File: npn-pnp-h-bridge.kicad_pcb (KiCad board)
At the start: 2 copper layers, 45 x 19 mm, 35 parts, among them J1 S4B-PH-K-S_LF__SN_, J2 S2B-PH-K-S_LF__SN_, Q1 MMDT3904, Q2 MMDT3904

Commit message: Add 1.0 revision number, use current screenshots, add exported case
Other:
- board text added: "${COMMENT1}"
- board text added: "H-Bridge for Fairylights ${REVISION}"
- board text removed: "H-Bridge for Fairylights"
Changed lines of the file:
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@@
 	)
 	(paper "A4")
+	(title_block
+		(rev "1.0")
+		(comment 1 "https://github.com/lk-ek/npn-pnp-h-bridge/")
+	)
 	(layers
 		(0 "F.Cu" signal)
@@
 		)
 	)
-	(gr_text "H-Bridge for Fairylights"
-		(at 110.83841 67.360437 0)
+	(gr_text "${COMMENT1}"
+		(at 110.2 51.2 0)
 		(layer "B.SilkS" knockout)
 		(effects
 			(font
-				(size 1 1)
+				(size 0.8 0.8)
+				(thickness 0.1)
+			)
+			(justify bottom mirror)
+		)
+	)
+	(gr_text "H-Bridge for Fairylights ${REVISION}"
+		(at 110.83841 67.6 0)
+		(layer "B.SilkS" knockout)
+		(effects
+			(font
+				(size 0.8 0.8)
 				(thickness 0.1)
 			)

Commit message: update pcb with new values
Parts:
- R11, R12: value 680 -> 2.2k
- R13, R14: value 100 -> 180

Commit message: first 4-layer try
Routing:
- net GND: track 6.69 -> 13.1 mm, vias 26 -> 10
- net /O2: track 4.20 -> 0.00 mm, vias 1 -> 0
- added copper zone on F.Cu, net /O1
- added copper zone on F.Cu, net /O2
- added copper zone on In1.Cu, net GND
- added copper zone on In2.Cu, net GND
- removed copper zone on F.Cu, net GND
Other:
- copper layers 2 -> 4

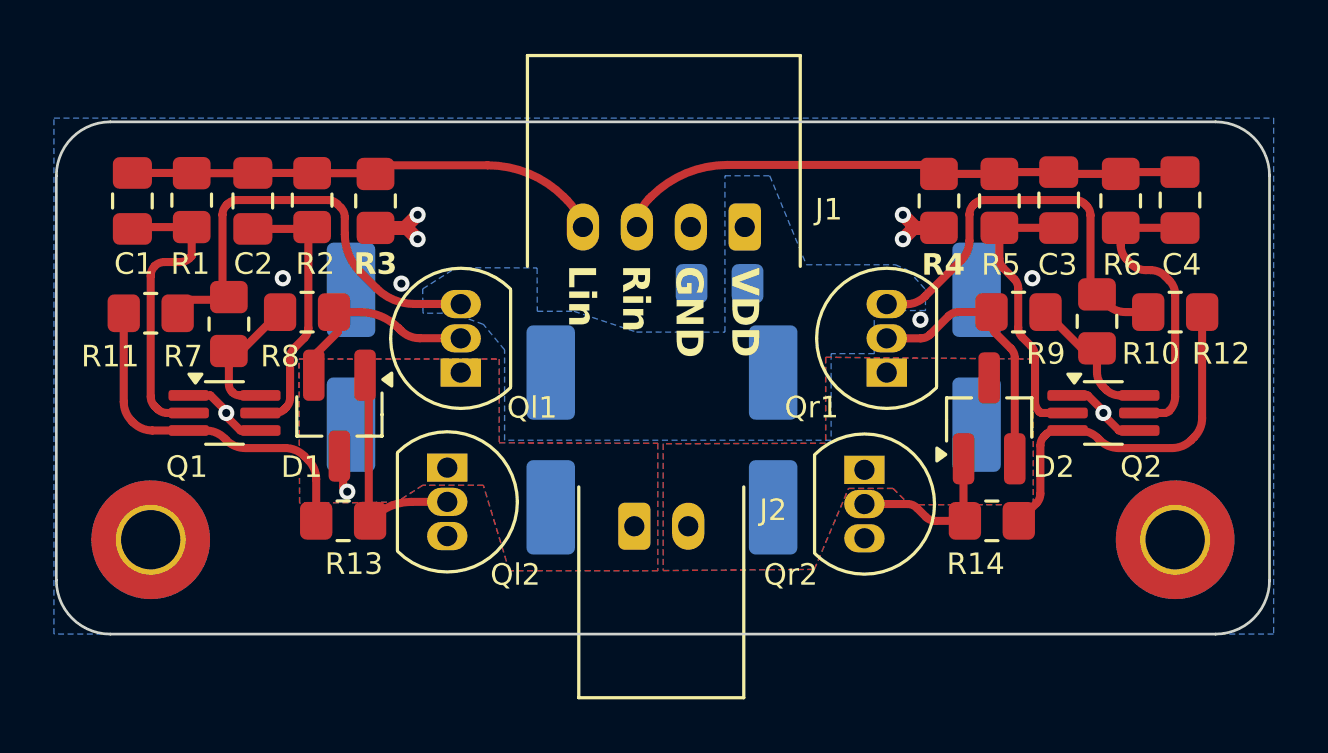
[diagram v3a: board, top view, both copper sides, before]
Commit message: finalize 4-layer design
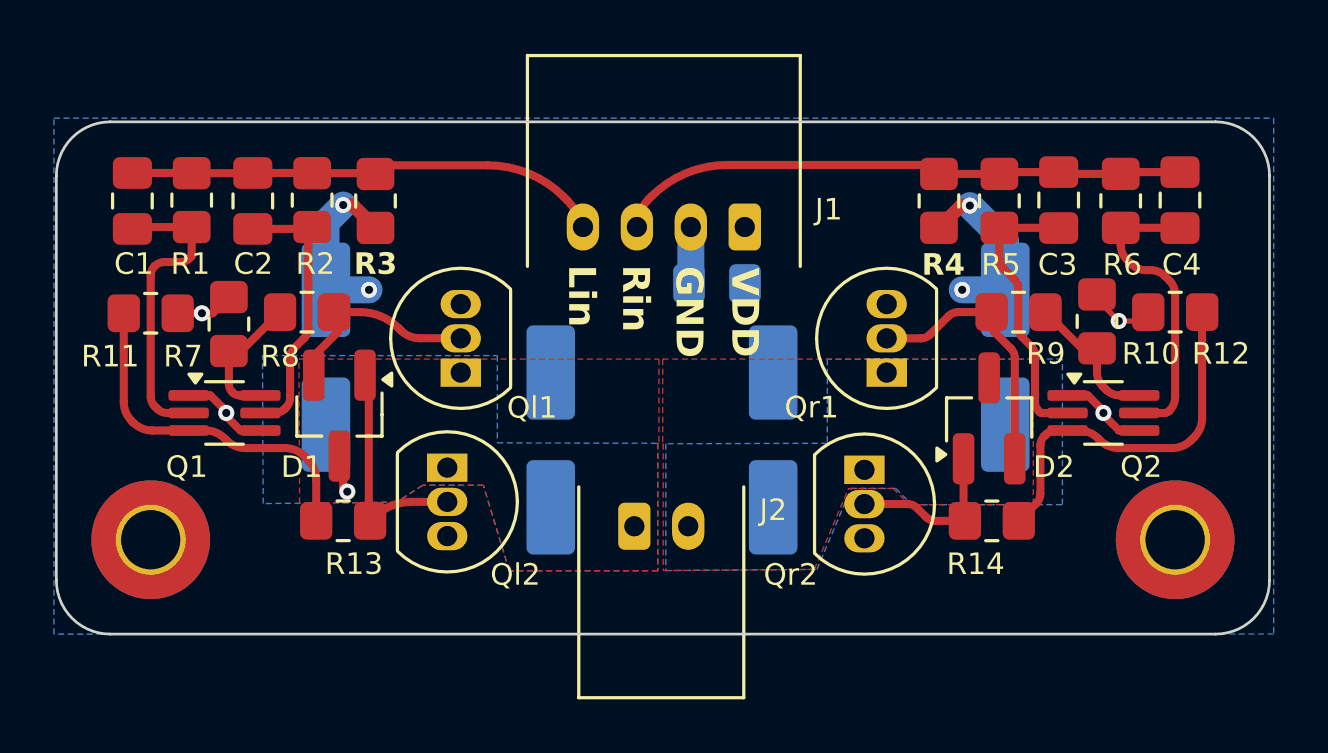
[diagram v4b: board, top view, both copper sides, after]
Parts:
- moved D3 1.07 mm to (123.6, 58.3)
- moved D4 0.93 mm to (98.4, 58.3)
- moved C5 0.10 mm to (112.9, 55.6)
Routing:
- net VDD: track 32.2 -> 4.70 mm, vias 0 -> 2
- net GND: track 13.1 -> 22.0 mm, vias 10 -> 6
- removed copper zone on B.Cu, net GND
